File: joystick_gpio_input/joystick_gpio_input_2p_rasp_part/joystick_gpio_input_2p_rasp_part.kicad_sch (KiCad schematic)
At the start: 3 parts, among them J11 Conn_01x13, J7 Conn_02x09_Odd_Even, J9 Conn_01x13

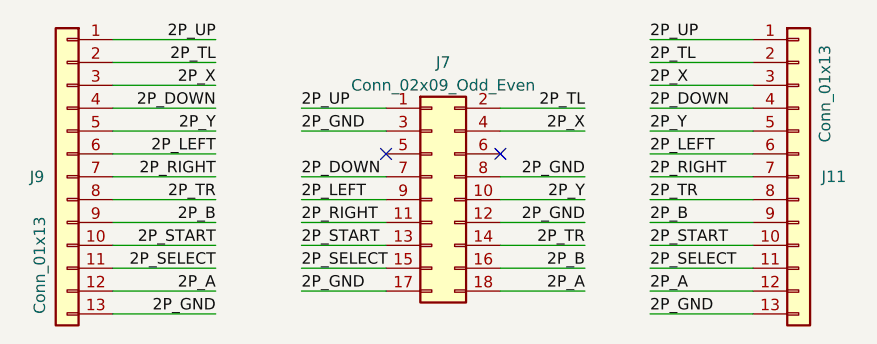
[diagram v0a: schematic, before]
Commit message: joystick gpio 스크린샷 추가
Signed-off-by: Ju, Gyeong-min <jcmh74@gmail.com>
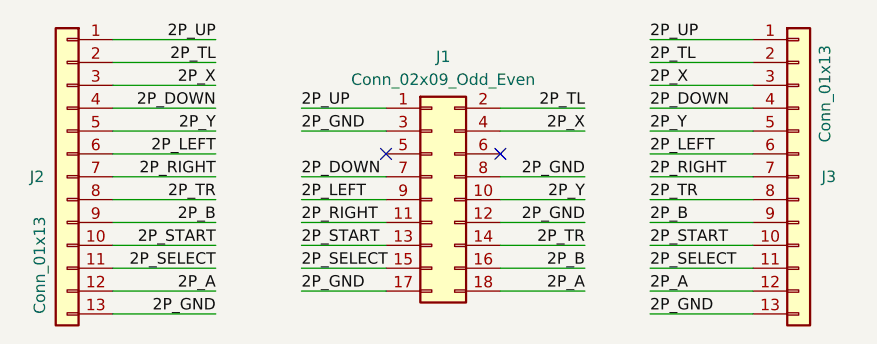
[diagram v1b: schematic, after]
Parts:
- renumbered J7 to J1, J9 to J2, J11 to J3
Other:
- title: Raspberry Pie GPIO Input Module -> Raspberry Pie GPIO Input Module (2P Part)
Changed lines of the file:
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@@
   (paper "A4")
   (title_block
-    (title "Raspberry Pie GPIO Input Module")
-    (date "2023-03-26")
+    (title "Raspberry Pie GPIO Input Module (2P Part)")
+    (date "2023-04-02")
     (rev "2")
     (company "Amos Home")
@@
   (symbol (lib_id "Connector_Generic:Conn_02x09_Odd_Even") (at 141.478 99.695 0) (unit 1)
     (in_bom yes) (on_board yes) (dnp no) (fields_autoplaced)
-    (property "Reference" "J7" (at 142.748 84.455 0)
+    (property "Reference" "J1" (at 142.748 83.82 0)
       (effects (font (size 1.27 1.27)))
     )
-    (property "Value" "Conn_02x09_Odd_Even" (at 142.748 86.995 0)
+    (property "Value" "Conn_02x09_Odd_Even" (at 142.748 86.36 0)
       (effects (font (size 1.27 1.27)))
     )
@@
       (project "joystick_gpio_input_2p_rasp_part"
         (path "/fa38296e-cdcc-4309-9d50-3ec5b62681ed"
-          (reference "J7") (unit 1)
+          (reference "J1") (unit 1)
         )
       )
@@
   (symbol (lib_id "Connector_Generic:Conn_01x13") (at 100.965 97.155 0) (mirror y) (unit 1)
     (in_bom yes) (on_board yes) (dnp no)
-    (property "Reference" "J9" (at 98.425 97.155 0)
+    (property "Reference" "J2" (at 98.425 97.155 0)
       (effects (font (size 1.27 1.27)) (justify left))
     )
@@
       (project "joystick_gpio_input_2p_rasp_part"
         (path "/fa38296e-cdcc-4309-9d50-3ec5b62681ed"
-          (reference "J9") (unit 1)
+          (reference "J2") (unit 1)
         )
       )
@@
   (symbol (lib_id "Connector_Generic:Conn_01x13") (at 182.245 97.155 0) (unit 1)
     (in_bom yes) (on_board yes) (dnp no)
-    (property "Reference" "J11" (at 184.785 97.155 0)
+    (property "Reference" "J3" (at 184.785 97.155 0)
       (effects (font (size 1.27 1.27)) (justify left))
     )
@@
       (project "joystick_gpio_input_2p_rasp_part"
         (path "/fa38296e-cdcc-4309-9d50-3ec5b62681ed"
-          (reference "J11") (unit 1)
+          (reference "J3") (unit 1)
         )
       )
